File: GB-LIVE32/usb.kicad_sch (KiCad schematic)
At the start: 6 parts

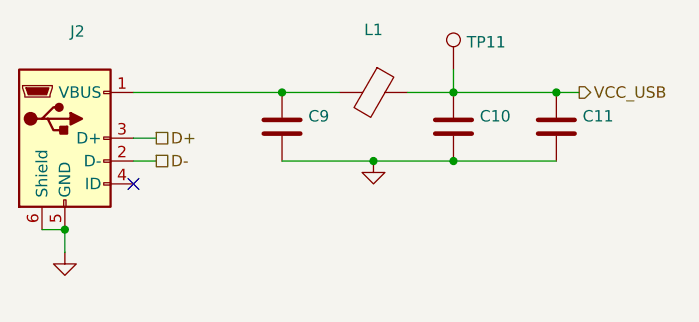
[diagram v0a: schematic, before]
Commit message: Upgrade projects to KiCad 7
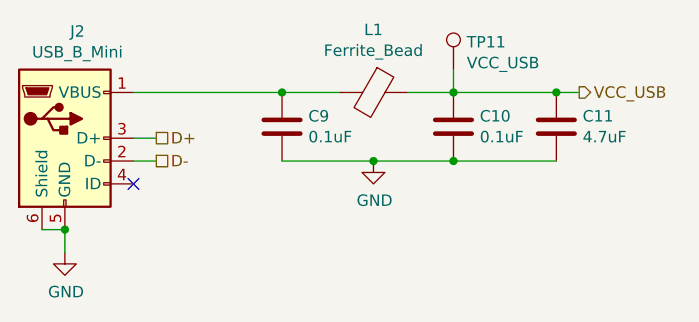
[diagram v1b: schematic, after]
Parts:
- C10, C9: value (none) -> 0.1uF; footprint (none) -> Capacitor_SMD:C_0603_1608Metric
- C11: value (none) -> 4.7uF; footprint (none) -> Capacitor_SMD:C_0805_2012Metric
- J2: value (none) -> USB_B_Mini; footprint (none) -> Gekkio_Connector_USB:USB_Mini-B_Hirose_UX60SC-MB-5ST80_Horizontal
- L1: value (none) -> Ferrite_Bead; footprint (none) -> Inductor_SMD:L_0603_1608Metric
- TP11: value (none) -> VCC_USB; footprint (none) -> TestPoint:TestPoint_Pad_D1.0mm
